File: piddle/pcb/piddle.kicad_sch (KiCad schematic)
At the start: 45 parts, among them J1 Conn_01x03_Socket, J10 Conn_01x03_Socket, J11 Conn_01x02_Socket, J12 Conn_01x02_Socket, J13 Conn_01x02_Pin, J2 Conn_01x03_Socket, J3 Conn_01x03_Socket, J4 Conn_01x03_Socket, J5 Conn_01x03_Socket, J6 Conn_01x03_Socket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

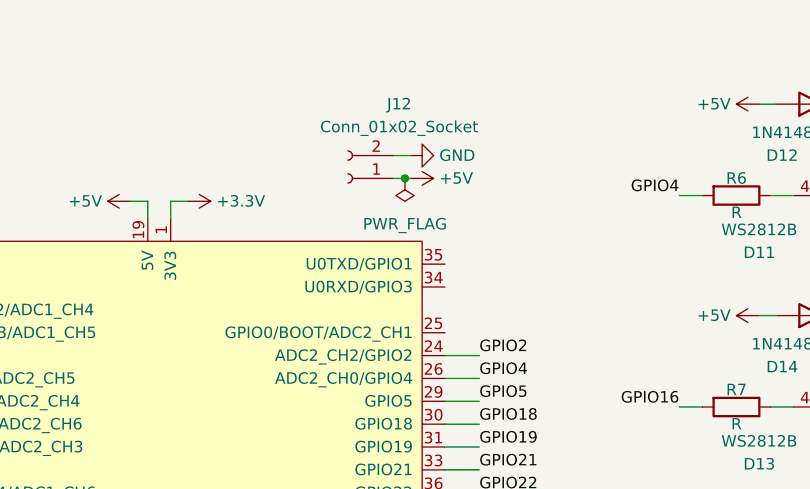
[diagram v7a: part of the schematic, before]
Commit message: More connections
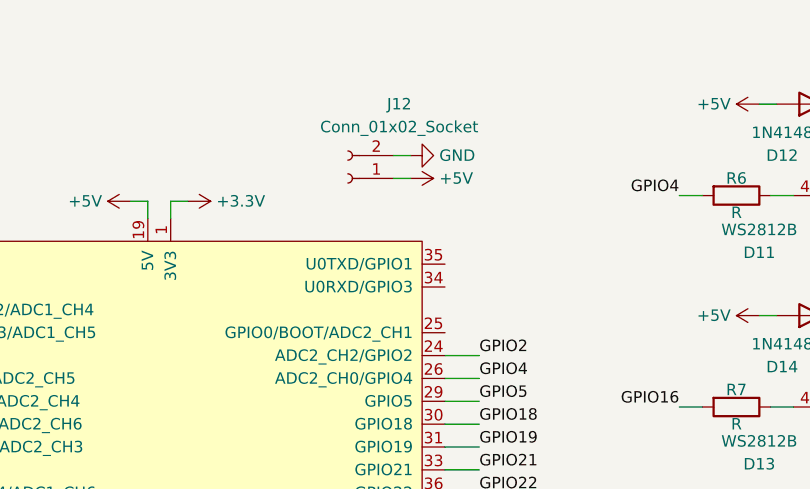
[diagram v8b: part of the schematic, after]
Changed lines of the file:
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@@
   (junction (at 112.395 45.085) (diameter 0) (color 0 0 0 0)
   )
-  (junction (at 168.275 45.085) (diameter 0) (color 0 0 0 0)
-  )
   (wire (pts (xy 172.72 87.63) (xy 176.53 87.63))
     (stroke (width 0) (type default))
@@
     (stroke (width 0) (type default))
   )
-  (wire (pts (xy 168.275 45.085) (xy 168.91 45.085))
-    (stroke (width 0) (type default))
-  )
   (wire (pts (xy 62.23 103.505) (xy 62.23 100.965))
     (stroke (width 0) (type default))
@@
     (stroke (width 0) (type default))
   )
-  (wire (pts (xy 167.005 45.085) (xy 168.275 45.085))
+  (wire (pts (xy 167.005 45.085) (xy 168.91 45.085))
     (stroke (width 0) (type default))
   )
@@
         )
       )
-    )
-  )
-  (symbol (lib_id "power:PWR_FLAG") (at 168.275 45.085 180) (unit 1)
-    (in_bom yes) (on_board yes) (dnp no) (fields_autoplaced)
-    (property "Reference" "#FLG02" (at 168.275 46.99 0)
-      (effects (font (size 1.27 1.27)) hide)
-    )
-    (property "Value" "PWR_FLAG" (at 168.275 50.165 0)
-      (effects (font (size 1.27 1.27)))
-    )
-    (property "Footprint" "" (at 168.275 45.085 0)
-      (effects (font (size 1.27 1.27)) hide)
-    )
-    (property "Datasheet" "~" (at 168.275 45.085 0)
-      (effects (font (size 1.27 1.27)) hide)
-    )
-    (pin "1")
-    (instances
-      (project "piddle"
-        (path "/08f3e99d-6a74-4a56-a078-a6f7466dafc2"
-          (reference "#FLG02") (unit 1)
-        )
-      )
